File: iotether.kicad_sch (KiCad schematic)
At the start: 54 parts, among them J101 USB_B_Micro, J102 Barrel_Jack, J103 Conn_02x04_Odd_Even, U101 LAN9514, U102 93CxxC, U103 LM1117-3.3, U104 MCP73831-2-OT, Y101 Crystal

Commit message: Add i2c_sampler, update to revision 3
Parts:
- added C126: C, Capacitor_SMD:C_0603_1608Metric, symbol Device:C
- added C127: C, Capacitor_THT:CP_Radial_D8.0mm_P3.80mm, symbol Device:C
- added L102: L, Inductor_SMD:L_1210_3225Metric_Pad1.42x2.65mm_HandSolder, symbol Device:L
- added R107: R, Resistor_SMD:R_0805_2012Metric, symbol Device:R
- added R108, R109: R, Resistor_SMD:R_0603_1608Metric, symbol Device:R
- added U105: AP62200, Package_TO_SOT_SMD:SOT-23-6, symbol Connector_Generic:Conn_02x03_Counter_Clockwise
- R106: footprint Resistor_SMD:R_0603_1608Metric_Pad1.05x0.95mm_HandSolder -> Resistor_SMD:R_0603_1608Metric_Pad0.98x0.95mm_HandSolder
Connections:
- net +3V3: now also L102.2, R108.1
- net +5V: now also C127.1, U105.3 (Pin_3), U105.5 (Pin_5)
- net GND: now also C127.2, R109.2, U105.1 (Pin_1)
- net at C101.1, U101.60 (XO), Y101.1: now also R107.1
- net at C103.1, U101.61 (XI), Y101.2: now also R107.2
- new net: R108.2, R109.1, U105.4 (Pin_4)
- new net: C126.1, L102.1, U105.2 (Pin_2)
- new net: C126.2, U105.6 (Pin_6)

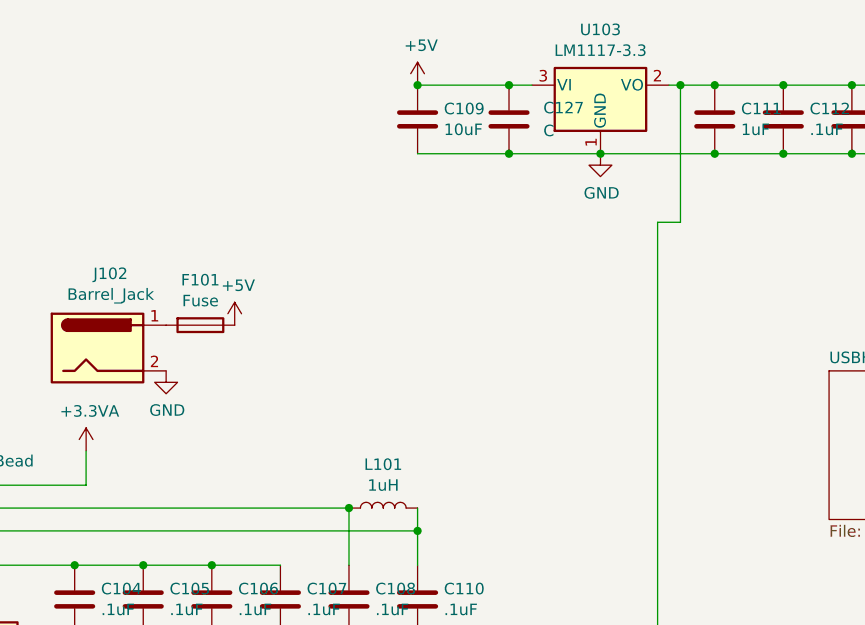
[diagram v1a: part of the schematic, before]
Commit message: Add 12V->5V regulator
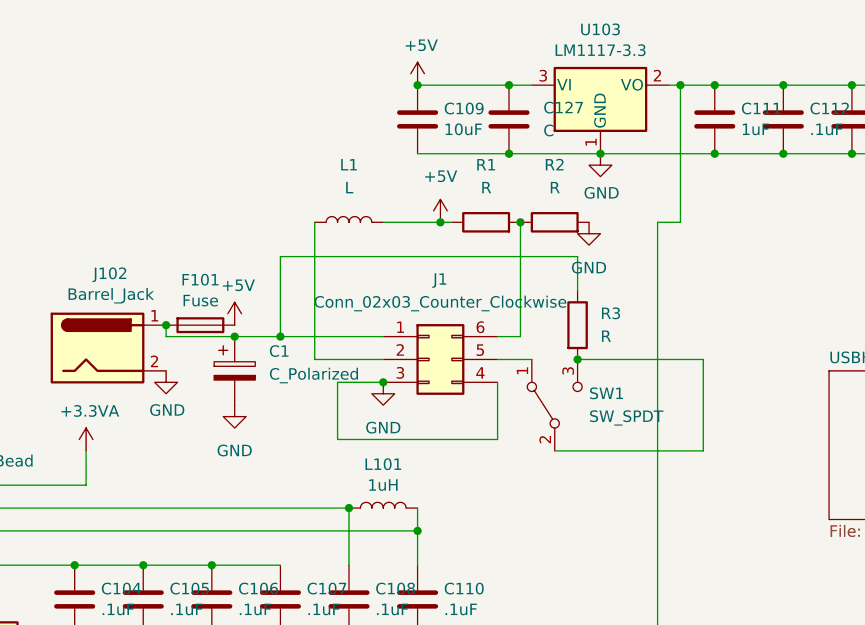
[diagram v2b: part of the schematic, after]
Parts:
- added C1: C_Polarized, Capacitor_THT:CP_Radial_D10.0mm_P5.00mm, symbol Device:C_Polarized
- added J1: Conn_02x03_Counter_Clockwise, Package_TO_SOT_SMD:SOT-563, symbol Connector_Generic:Conn_02x03_Counter_Clockwise
- added L1: L, Inductor_THT:L_Radial_D12.5mm_P7.00mm_Fastron_09HCP, symbol Device:L
- added R1, R2, R3: R, Resistor_SMD:R_0603_1608Metric, symbol Device:R
- added SW1: SW_SPDT, Connector_PinSocket_2.54mm:PinSocket_1x03_P2.54mm_Vertical, symbol Switch:SW_SPDT
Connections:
- net +5V: now also L1.2, R1.1
- net GND: now also C1.2, J1.3 (Pin_3), J1.4 (Pin_4), R2.2
- net at F101.2, J102.1: now also C1.1, J1.1 (Pin_1), R3.1
- new net: J1.2 (Pin_2), L1.1
- new net: J1.6 (Pin_6), R1.2, R2.1
- new net: R3.2, SW1.2 (B), SW1.3 (C)
- new net: J1.5 (Pin_5), SW1.1 (A)

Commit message: IoTether: Add USB-C
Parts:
- removed J101: USB_B_Micro, Connector_PinHeader_2.54mm:PinHeader_1x06_P2.54mm_Vertical, symbol iotether-rescue:USB_B_Micro-Connector
- added J101: USB_C_Receptacle_USB2.0, Library:USB_C_Receptacle_GCT_USB4105-xx-A_16P_TopMnt_Horizontal, symbol Connector:USB_C_Receptacle_USB2.0
- added R110, R111: R, Resistor_SMD:R_0603_1608Metric, symbol Device:R
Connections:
- net GND: now also J101.A1 (GND), J101.A12 (GND), J101.B1 (GND), J101.B12 (GND), J101.S1 (SHIELD), R110.2, R111.2
- net UP_D+: now also J101.A6 (D+), J101.B6 (D+)
- net UP_D-: now also J101.A7 (D-), J101.B7 (D-)
- net VBUS: now also J101.A4 (VBUS), J101.A9 (VBUS), J101.B4 (VBUS), J101.B9 (VBUS)
- new net: J101.A5 (CC1), R110.1
- new net: J101.B5 (CC2), R111.1
